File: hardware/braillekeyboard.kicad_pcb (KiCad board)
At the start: 2 copper layers, 33 parts, among them J1 Conn_01x15_Socket, J2 Conn_01x15_Socket, Q1 BC337, Q2 BC337, Q3 BC337, Q4 BC337, Q5 BC337, Q6 BC337, U1 LM2596

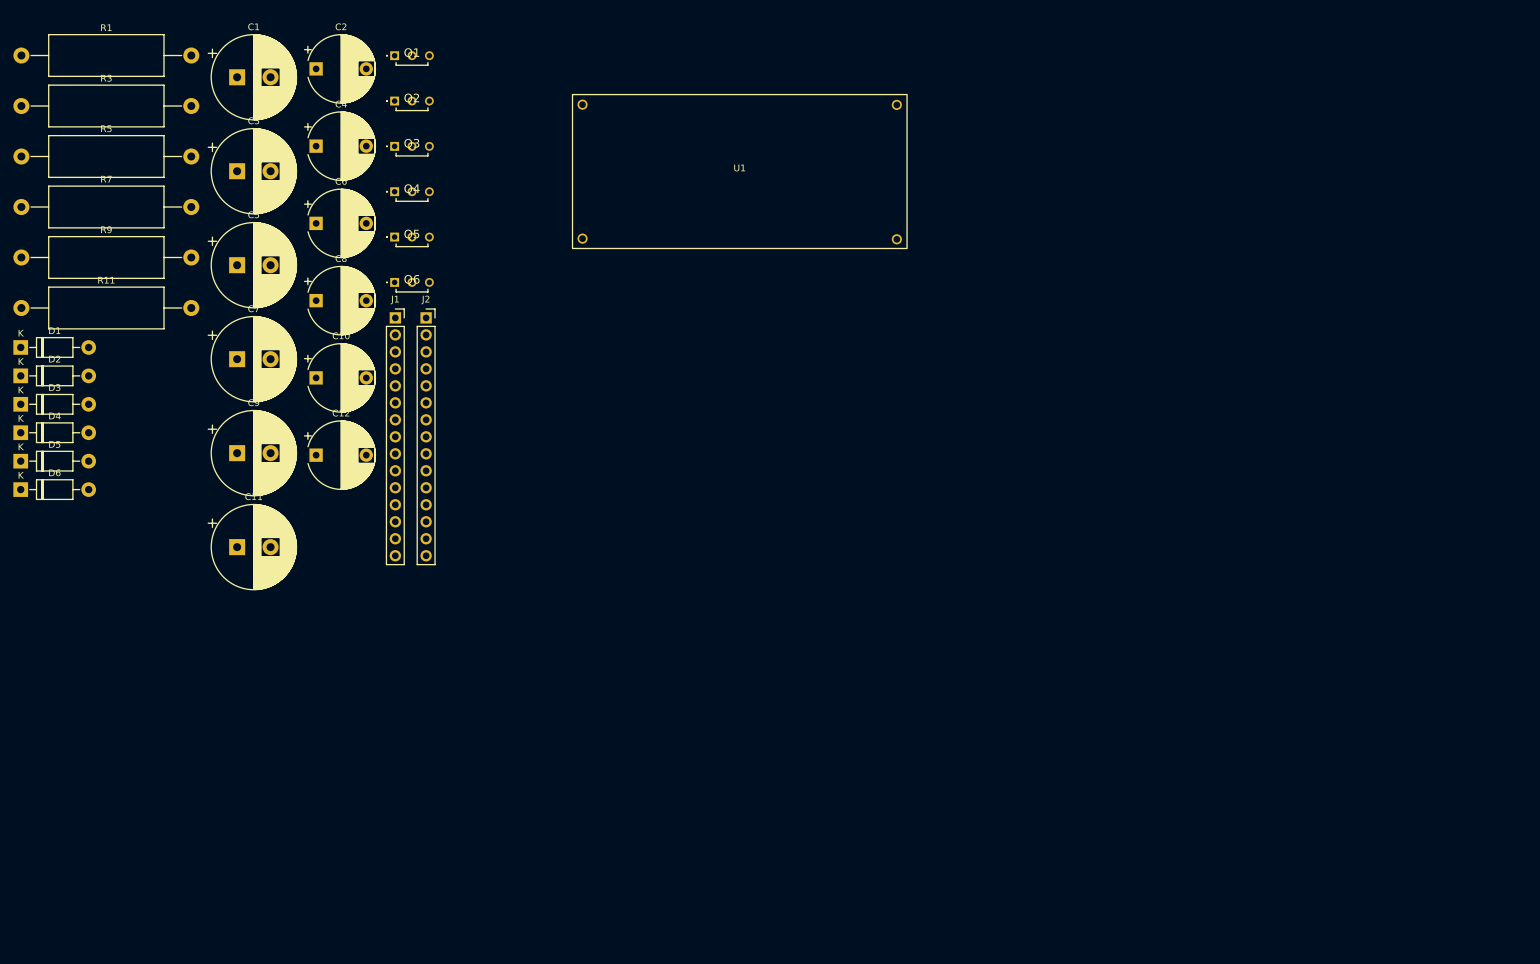
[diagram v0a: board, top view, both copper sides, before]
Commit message: Reorganização dos componentes
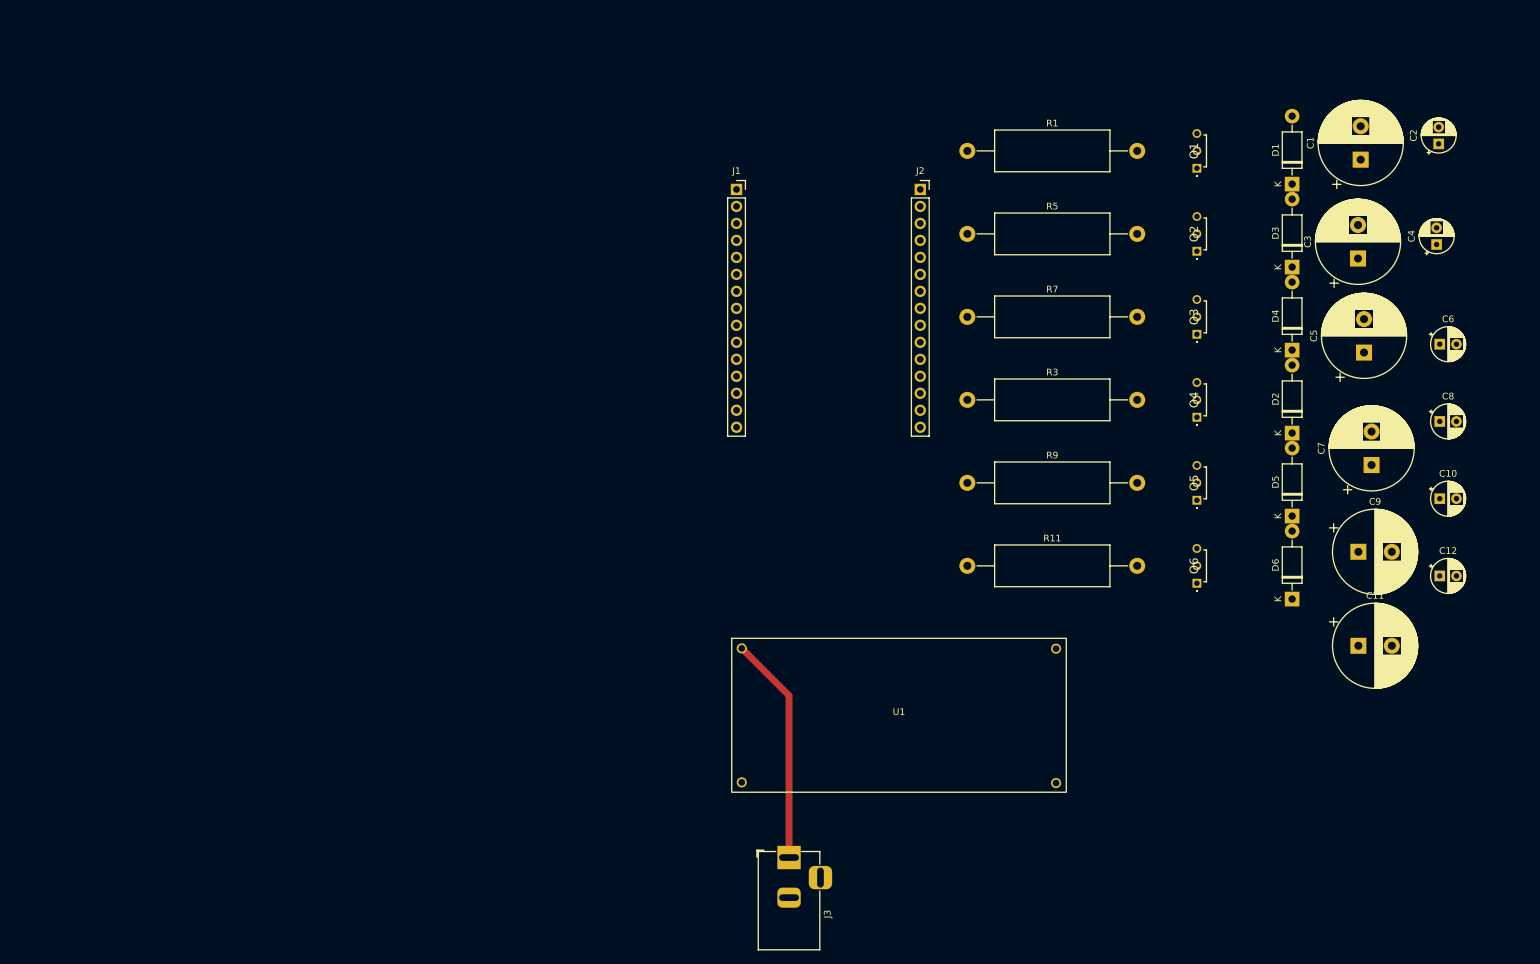
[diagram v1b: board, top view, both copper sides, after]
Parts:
- added J3: Barrel_Jack_Switch, barreljack:BarrelJack_Horizontal, F.Cu at (138.6, 142.4)
- C10, C12, C2, C4, C6, C8: footprint Capacitor_THT:CP_Radial_D10.0mm_P7.50mm -> Capacitor_THT:CP_Radial_D5.0mm_P2.50mm
- moved D1 191.7 mm to (213.8, 41.7), turned to 90 degrees
- moved D3 191.2 mm to (213.8, 54.1), turned to 90 degrees
- moved D6 190.8 mm to (213.8, 103.7), turned to 90 degrees
- moved D4 190.5 mm to (213.8, 66.5), turned to 90 degrees
- moved D2 190.3 mm to (213.8, 78.9), turned to 90 degrees
- moved D5 190.3 mm to (213.8, 91.3), turned to 90 degrees
- moved C7 170.4 mm to (225.7, 83.7), turned to 90 degrees
- moved C5 169.0 mm to (224.6, 66.9), turned to 90 degrees
- moved C12 169.0 mm to (235.9, 100.3)
- moved C6 169.0 mm to (235.9, 65.6)
- moved C8 169.0 mm to (235.9, 77.2)
- moved C10 169.0 mm to (235.9, 88.7)
- moved C1 168.4 mm to (224.1, 38.1), turned to 90 degrees
- moved C11 168.3 mm to (223.7, 110.7)
- moved C9 168.3 mm to (223.7, 96.7)
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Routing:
- net VCC12: track 0.00 -> 34.2 mm

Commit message: PCB layout v1
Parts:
- added M1: Motor_DC, Connector_JST:JST_XH_B2B-XH-AM_1x02_P2.50mm_Vertical, F.Cu at (241.5, 31.8)
- added M2: Motor_DC, Connector_JST:JST_XH_B2B-XH-AM_1x02_P2.50mm_Vertical, F.Cu at (241.5, 46.9)
- added M3: Motor_DC, Connector_JST:JST_XH_B2B-XH-AM_1x02_P2.50mm_Vertical, F.Cu at (241.5, 61.7)
- added M4: Motor_DC, Connector_JST:JST_XH_B2B-XH-AM_1x02_P2.50mm_Vertical, F.Cu at (241.5, 76.9)
- added M5: Motor_DC, Connector_JST:JST_XH_B2B-XH-AM_1x02_P2.50mm_Vertical, F.Cu at (241.5, 91.9)
- added M6: Motor_DC, Connector_JST:JST_XH_B2B-XH-AM_1x02_P2.50mm_Vertical, F.Cu at (241.5, 106.9)
- moved J3 114.5 mm to (116.4, 30.0), turned to -90 degrees
- moved J2 35.6 mm to (158.2, 78.1), turned to 180 degrees
- moved D4 26.3 mm to (234.4, 82.9), turned to 0 degrees
- moved U1 24.6 mm to (138.3, 103.1)
- moved D3 23.4 mm to (234.4, 68.0), turned to 0 degrees
- moved D6 22.5 mm to (234.4, 112.8), turned to 0 degrees
- moved D5 21.6 mm to (234.4, 97.8), turned to 0 degrees
- moved D1 20.9 mm to (234.4, 38.1), turned to 0 degrees
- moved D2 20.6 mm to (234.4, 53.0), turned to 0 degrees
- moved C3 20.2 mm to (222.3, 46.9)
- moved C4 18.8 mm to (234.4, 46.9), turned to 90 degrees
- moved Q3 18.0 mm to (210.1, 62.0)
- moved R3 18.0 mm to (175.8, 59.4)
- moved R4 16.6 mm to (175.8, 74.4)
- moved Q4 16.6 mm to (210.1, 77.0)
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- renumbered C5 to C3, C6 to C4, C3 to C5, C4 to C6, D3 to D2, D2 to D3, Q4 to Q3, Q3 to Q4, R5 to R2, R7 to R4, R9 to R5, R11 to R6
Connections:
- R2 pad 1: D5 -> D19
- R3 pad 1: D19 -> D18
- R4 pad 1: D17 -> D5
- R5 pad 1: D18 -> D17
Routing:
- net VCC7_5: track 0.00 -> 380.7 mm
- net D16: track 0.00 -> 46.3 mm
- net D17: track 0.00 -> 36.2 mm
- net D21: track 0.00 -> 30.6 mm
- net VCC12: track 34.2 -> 63.7 mm
- net D5: track 0.00 -> 25.7 mm
- net D19: track 0.00 -> 22.1 mm
- net D18: track 0.00 -> 18.2 mm
- net Net-(Q6-B): track 0.00 -> 8.92 mm
- net Net-(Q5-B): track 0.00 -> 8.92 mm
- net Net-(Q4-B): track 0.00 -> 8.92 mm
- net Net-(Q3-B): track 0.00 -> 8.92 mm
- net Net-(Q2-B): track 0.00 -> 8.92 mm
- net Net-(Q1-B): track 0.00 -> 8.92 mm
- added copper zone on B.Cu, net GND
- added copper zone on F.Cu, net GND
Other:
- board outline added: 140.1 x 95.9 mm
- board text added: "Alcima"
